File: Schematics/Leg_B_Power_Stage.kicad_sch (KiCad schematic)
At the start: 40 parts, among them Q4 C3M0025065K, Q5 C3M0025065K, U3 UCC21710QDWRQ1, U4 UCC21710QDWRQ1

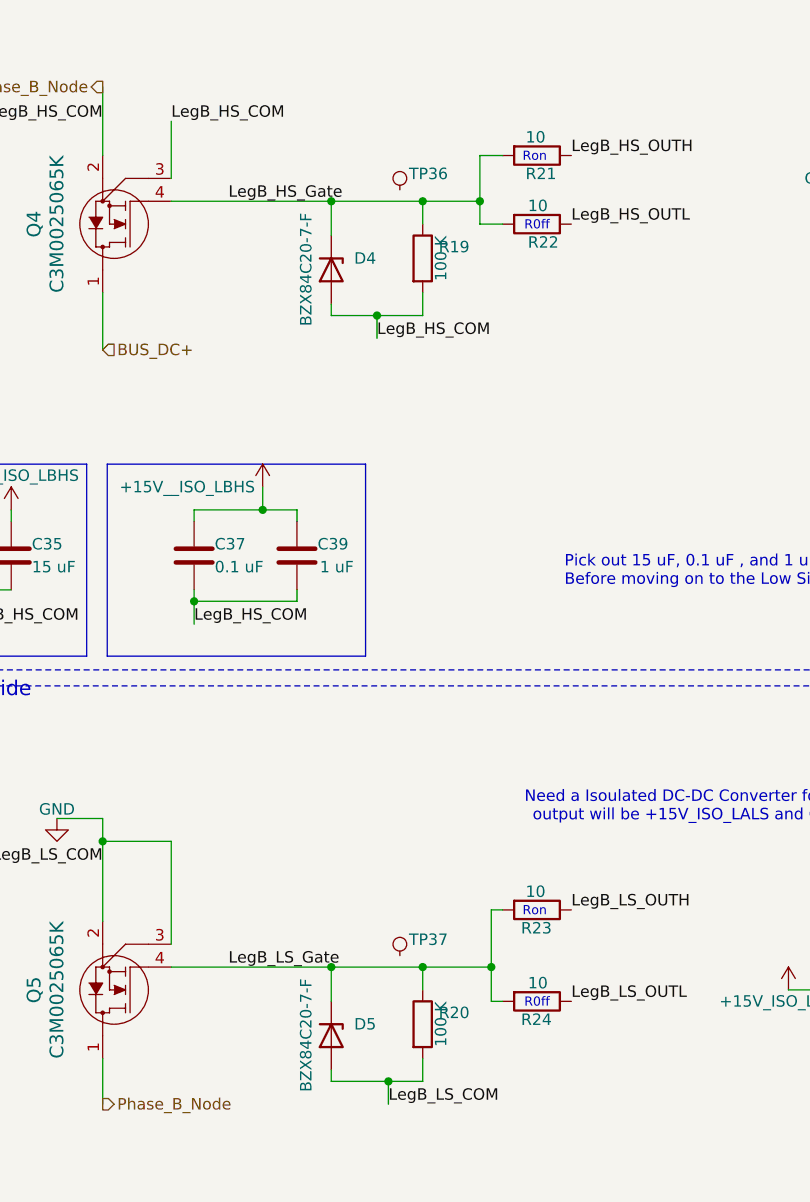
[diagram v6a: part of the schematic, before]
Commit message: Finished Full Bridge Layout
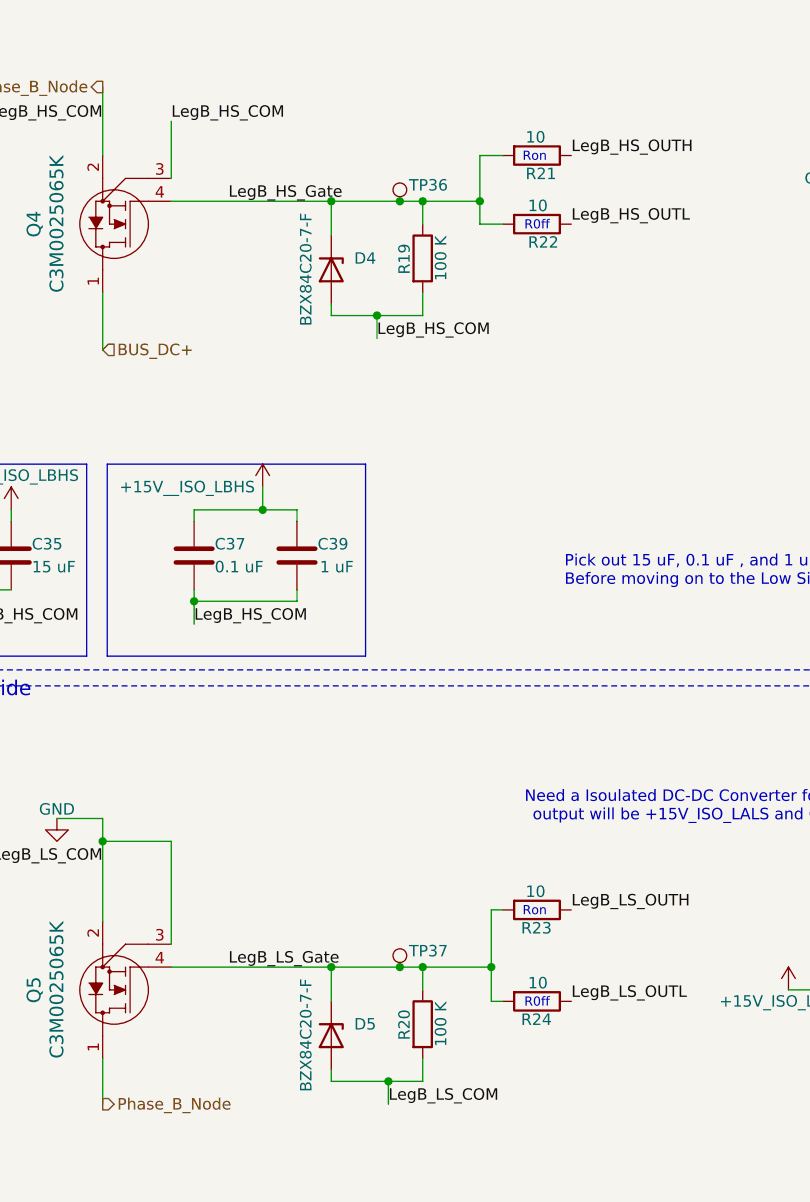
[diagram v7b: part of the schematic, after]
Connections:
- net LegB_HS_Gate: now also TP36.1
- net LegB_LS_Gate: now also TP37.1
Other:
- moved on the sheet: TP36, TP37
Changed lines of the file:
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@@
 	)
 	(junction
+		(at 67.31 139.7)
+		(diameter 0)
+		(color 0 0 0 0)
+	)
+	(junction
 		(at 207.01 142.24)
 		(diameter 0)
@@
 	)
 	(junction
+		(at 67.31 54.61)
+		(diameter 0)
+		(color 0 0 0 0)
+	)
+	(junction
 		(at 44.45 186.69)
 		(diameter 0)
@@
 	(wire
 		(pts
-			(xy 59.69 54.61) (xy 69.85 54.61)
+			(xy 59.69 54.61) (xy 67.31 54.61)
 		)
 		(stroke
@@
 	(wire
 		(pts
+			(xy 67.31 54.61) (xy 69.85 54.61)
+		)
+		(stroke
+			(width 0)
+			(type default)
+		)
+	)
+	(wire
+		(pts
 			(xy 69.85 152.4) (xy 66.04 152.4)
 		)
@@
 	(wire
 		(pts
+			(xy 67.31 139.7) (xy 69.85 139.7)
+		)
+		(stroke
+			(width 0)
+			(type default)
+		)
+	)
+	(wire
+		(pts
 			(xy 41.91 54.61) (xy 59.69 54.61)
 		)
@@
 	(wire
 		(pts
-			(xy 59.69 139.7) (xy 69.85 139.7)
+			(xy 59.69 139.7) (xy 67.31 139.7)
 		)
 		(stroke
@@
 		(dnp no)
 		(property "Reference" "R19"
-			(at 71.628 59.69 0)
+			(at 67.818 62.738 90)
 			(show_name no)
 			(do_not_autoplace no)
@@
 		(dnp no)
 		(property "Reference" "R20"
-			(at 71.628 144.78 0)
+			(at 67.818 147.828 90)
 			(show_name no)
 			(do_not_autoplace no)
@@
 	(symbol
 		(lib_id "SiC_Inverter:5277")
-		(at 67.31 139.7 0)
+		(at 67.31 140.97 0)
 		(unit 1)
 		(body_style 1)
@@
 		(dnp no)
 		(property "Reference" "TP37"
-			(at 68.326 136.652 0)
+			(at 68.326 137.922 0)
 			(show_name no)
 			(do_not_autoplace no)
@@
 		)
 		(property "Value" "5277"
-			(at 51.308 152.654 0)
+			(at 51.308 153.924 0)
 			(hide yes)
 			(show_name no)
@@
 		)
 		(property "Footprint" "SiC_Inverter:5277"
-			(at 57.404 150.876 0)
+			(at 57.404 152.146 0)
 			(hide yes)
 			(show_name no)
@@
 		)
 		(property "Datasheet" "https://www.keyelco.com/userAssets/file/K75p62.pdf"
-			(at 75.184 147.066 0)
+			(at 75.184 148.336 0)
 			(hide yes)
 			(show_name no)
@@
 		)
 		(property "Description" "Test Plugs & Test Jacks TEST POINT (BLUE) - COMPACT"
-			(at 77.724 149.098 0)
+			(at 77.724 150.368 0)
 			(hide yes)
 			(show_name no)
@@
 	(symbol
 		(lib_id "SiC_Inverter:5277")
-		(at 67.31 54.61 0)
+		(at 67.31 55.88 0)
 		(unit 1)
 		(body_style 1)
@@
 		(dnp no)
 		(property "Reference" "TP36"
-			(at 68.326 51.562 0)
+			(at 68.326 52.832 0)
 			(show_name no)
 			(do_not_autoplace no)
@@
 		)
 		(property "Value" "5277"
-			(at 51.308 67.564 0)
+			(at 51.308 68.834 0)
 			(hide yes)
 			(show_name no)
@@
 		)
 		(property "Footprint" "SiC_Inverter:5277"
-			(at 57.404 65.786 0)
+			(at 57.404 67.056 0)
 			(hide yes)
 			(show_name no)
@@
 		)
 		(property "Datasheet" "https://www.keyelco.com/userAssets/file/K75p62.pdf"
-			(at 75.184 61.976 0)
+			(at 75.184 63.246 0)
 			(hide yes)
 			(show_name no)
@@
 		)
 		(property "Description" "Test Plugs & Test Jacks TEST POINT (BLUE) - COMPACT"
-			(at 77.724 64.008 0)
+			(at 77.724 65.278 0)
 			(hide yes)
 			(show_name no)
